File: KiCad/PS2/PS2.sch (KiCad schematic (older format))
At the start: 6 parts, among them J1 Conn_01x06

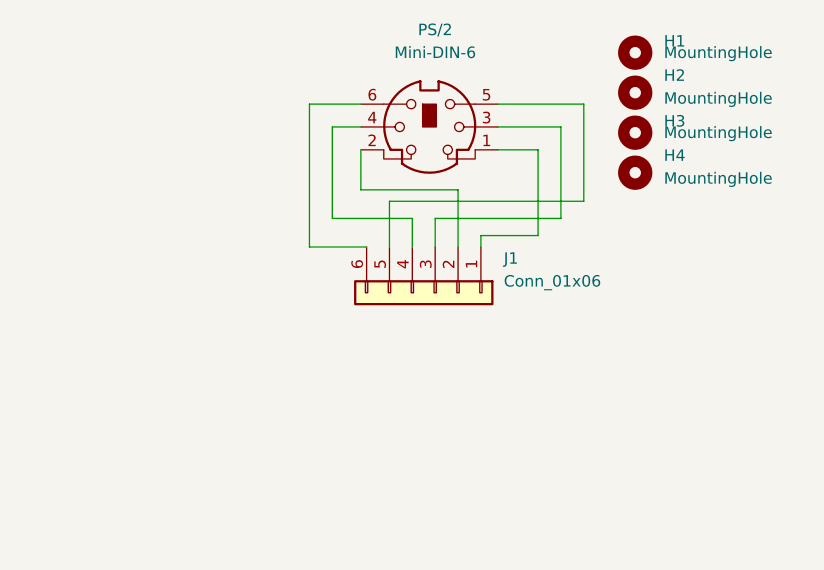
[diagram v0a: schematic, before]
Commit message: Update STM8 PS/2 device scanner. Optmise Keysearch, use interupts in send to all MTing. add possible PS2 test board.
Signed-off-by: John Bradley <flypie@rocketmail.com>
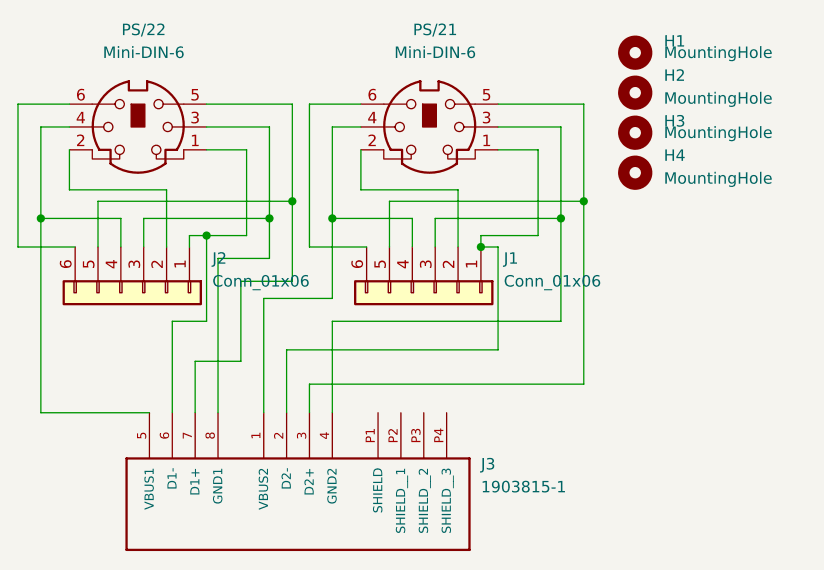
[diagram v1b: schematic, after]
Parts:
- added J2: Conn_01x06, Connector_PinSocket_2.54mm:PinSocket_1x06_P2.54mm_Vertical, symbol Connector_Generic:Conn_01x06
- added J3: 1903815-1, TE_1903815-1, symbol 1903815-1:1903815-1
- added PS/22: Mini-DIN-6, Local:5749180-1, symbol Connector:Mini-DIN-6
- renumbered PS/2 to PS/21
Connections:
- net at J1.1 (Pin_1), PS/21.1: now also J3.2 (D2-)
- net at J1.3 (Pin_3), PS/21.3: now also J3.4 (GND2)
- net at J1.4 (Pin_4), PS/21.4: now also J3.1 (VBUS2)
- net at J1.5 (Pin_5), PS/21.5: now also J3.3 (D2+)
- new net: J2.1 (Pin_1), J3.6 (D1-), PS/22.1
- new net: J2.2 (Pin_2), PS/22.2
- new net: J2.3 (Pin_3), J3.8 (GND1), PS/22.3
- new net: J2.4 (Pin_4), J3.5 (VBUS1), PS/22.4
- new net: J2.5 (Pin_5), J3.7 (D1+), PS/22.5
- new net: J2.6 (Pin_6), PS/22.6
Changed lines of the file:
@@
 $EndDescr
 $Comp
-L Connector:Mini-DIN-6 PS/2
+L Connector:Mini-DIN-6 PS/21
 U 1 1 5DE69561
 P 5275 2525
-F 0 "PS/2" H 5300 2950 50  0000 C CNN
+F 0 "PS/21" H 5300 2950 50  0000 C CNN
 F 1 "Mini-DIN-6" H 5300 2850 50  0000 C CNN
 F 2 "Local:5749180-1" H 5275 2525 50  0001 C CNN
@@
 	5500 3050 5500 3000
 Wire Wire Line
-	5500 3000 5750 3000
-Wire Wire Line
 	5750 3000 5750 2625
 Wire Wire Line
@@
 	1    0    0    -1
 $EndComp
+$Comp
+L Connector:Mini-DIN-6 PS/22
+U 1 1 5E0946EF
+P 4000 2525
+F 0 "PS/22" H 4025 2950 50  0000 C CNN
+F 1 "Mini-DIN-6" H 4025 2850 50  0000 C CNN
+F 2 "Local:5749180-1" H 4000 2525 50  0001 C CNN
+F 3 "http://service.powerdynamics.com/ec/Catalog17/Section%2011.pdf" H 4000 2525 50  0001 C CNN
+	1    4000 2525
+	1    0    0    -1
+$EndComp
+$Comp
+L Connector_Generic:Conn_01x06 J2
+U 1 1 5E0946F9
+P 4025 3250
+F 0 "J2" V 3875 3550 50  0000 L CNN
+F 1 "Conn_01x06" V 3975 3550 50  0000 L CNN
+F 2 "Connector_PinSocket_2.54mm:PinSocket_1x06_P2.54mm_Vertical" H 4025 3250 50  0001 C CNN
+F 3 "~" H 4025 3250 50  0001 C CNN
+	1    4025 3250
+	0    1    1    0
+$EndComp
+Wire Wire Line
+	4225 3050 4225 3000
+Wire Wire Line
+	4225 3000 4300 3000
+Wire Wire Line
+	4475 3000 4475 2625
+Wire Wire Line
+	4475 2625 4300 2625
+Wire Wire Line
+	4125 3050 4125 2800
+Wire Wire Line
+	4125 2800 3700 2800
+Wire Wire Line
+	3700 2800 3700 2625
+Wire Wire Line
+	4025 3050 4025 2925
+Wire Wire Line
+	4025 2925 4575 2925
+Wire Wire Line
+	4575 2925 4575 2525
+Wire Wire Line
+	4575 2525 4300 2525
+Wire Wire Line
+	3925 3050 3925 2925
+Wire Wire Line
+	3925 2925 3575 2925
+Wire Wire Line
+	3575 2925 3575 2525
+Wire Wire Line
+	3575 2525 3700 2525
+Wire Wire Line
+	3825 3050 3825 2850
+Wire Wire Line
+	3825 2850 4675 2850
+Wire Wire Line
+	4675 2850 4675 2425
+Wire Wire Line
+	4675 2425 4300 2425
+Wire Wire Line
+	3725 3050 3475 3050
+Wire Wire Line
+	3475 3050 3475 2425
+Wire Wire Line
+	3475 2425 3700 2425
+Wire Wire Line
+	3575 2925 3575 3775
+Wire Wire Line
+	3575 3775 4050 3775
+Connection ~ 3575 2925
+Wire Wire Line
+	4850 2925 4850 3275
+Wire Wire Line
+	4850 3275 4550 3275
+Connection ~ 4850 2925
+Wire Wire Line
+	4575 2925 4575 3100
+Wire Wire Line
+	4575 3100 4350 3100
+Connection ~ 4575 2925
+Wire Wire Line
+	5850 2925 5850 3375
+Wire Wire Line
+	5850 3375 4850 3375
+Connection ~ 5850 2925
+Connection ~ 4300 3000
+Wire Wire Line
+	4300 3000 4475 3000
+Wire Wire Line
+	5500 3050 5575 3050
+Wire Wire Line
+	5575 3050 5575 3500
+Wire Wire Line
+	5575 3500 4650 3500
+Connection ~ 5500 3050
+Wire Wire Line
+	4300 3375 4150 3375
+Wire Wire Line
+	4850 3375 4850 3775
+Wire Wire Line
+	4750 3650 4750 3775
+Wire Wire Line
+	4650 3500 4650 3775
+Wire Wire Line
+	4550 3275 4550 3775
+Wire Wire Line
+	4350 3100 4350 3775
+Wire Wire Line
+	4300 3000 4300 3375
+Wire Wire Line
+	4150 3375 4150 3775
+$Comp
+L 1903815-1:1903815-1 J3
+U 1 1 5E098547
+P 4450 4175
+F 0 "J3" V 4625 3125 50  0000 R CNN
+F 1 "1903815-1" V 4525 3125 50  0000 R CNN
+F 2 "TE_1903815-1" H 4450 4175 50  0001 L BNN
+F 3 "1903815-1" H 4450 4175 50  0001 L BNN
+F 4 "https://www.te.com/usa-en/product-1903815-1.html?te_bu=Cor&te_type=disp&te_campaign=seda_glo_cor-seda-global-disp-prtnr-fy19-seda-model-bom-cta_sma-317_1&elqCampaignId=32493" H 4450 4175 50  0001 L BNN "Field4"
+	1    4450 4175
+	0    -1   -1   0
+$EndComp
+Wire Wire Line
+	4675 2850 4675 3200
+Wire Wire Line
+	4675 3200 4450 3200
+Wire Wire Line
+	4450 3200 4450 3550
+Wire Wire Line
+	4450 3550 4250 3550
+Wire Wire Line
+	4250 3550 4250 3775
+Connection ~ 4675 2850
+Wire Wire Line
+	5500 3000 5750 3000
+Wire Wire Line
+	5950 2850 5950 3650
+Wire Wire Line
+	4750 3650 5950 3650
+Connection ~ 5950 2850
 $EndSCHEMATC
